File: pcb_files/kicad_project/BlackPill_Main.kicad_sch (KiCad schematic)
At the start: 2 parts

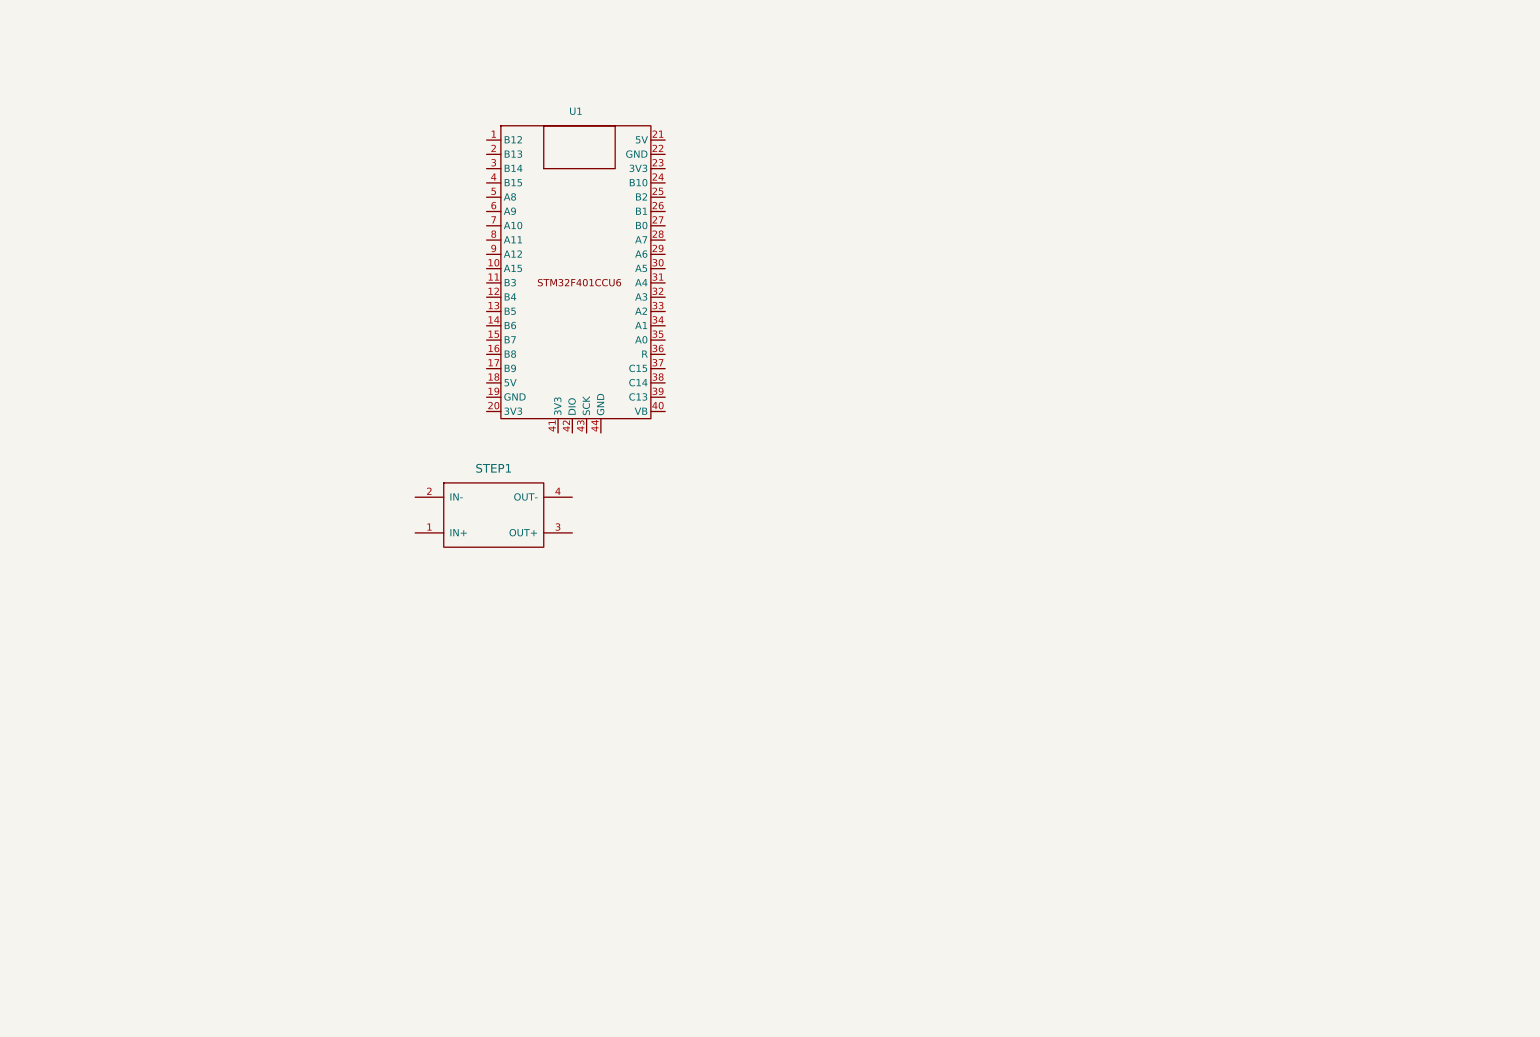
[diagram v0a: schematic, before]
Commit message: Añade pinout de BlackPill, completa esquemático y asocia footprints
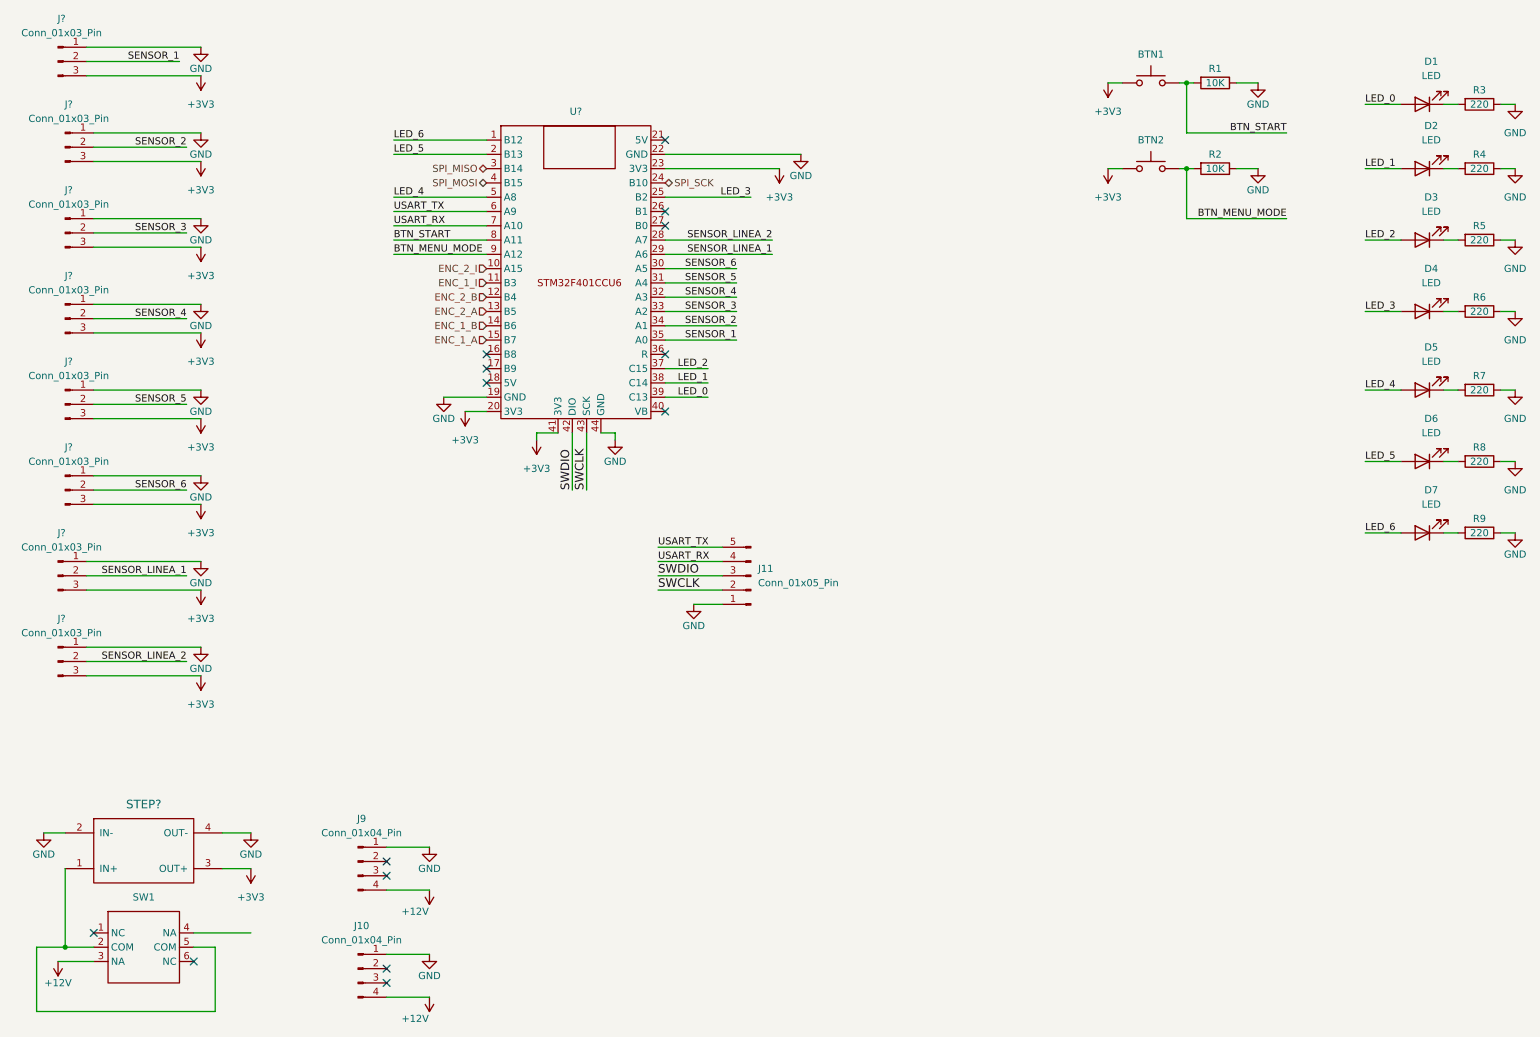
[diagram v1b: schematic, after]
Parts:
- added BTN1, BTN2: ~, Button_Switch_SMD:SW_SPST_EVQPE1, symbol custom_libraries:Button
- added D1, D2, D3, D4, D5, D6, D7: LED, LED_SMD:LED_0805_2012Metric, symbol Device:LED
- added J10, J9: Conn_01x04_Pin, Connector_PinHeader_2.54mm:PinHeader_1x04_P2.54mm_Vertical, symbol Connector:Conn_01x04_Pin
- added J11: Conn_01x05_Pin, Connector_PinHeader_2.54mm:PinHeader_1x05_P2.54mm_Vertical, symbol Connector:Conn_01x05_Pin
- added J? (x8): Conn_01x03_Pin, Connector_PinHeader_2.54mm:PinHeader_1x03_P2.54mm_Vertical, symbol Connector:Conn_01x03_Pin
- added R1, R2: 10K, Resistor_SMD:R_0805_2012Metric_Pad1.20x1.40mm_HandSolder, symbol Device:R
- added R3, R4, R5, R6, R7, R8, R9: 220, Resistor_SMD:R_0805_2012Metric_Pad1.20x1.40mm_HandSolder, symbol Device:R
- added SW1: ~, custom_library:Switch6P, symbol custom_libraries:Switch
- STEP?: renamed from STEP1; footprint (none) -> custom_library:Mini360
- U?: renamed from U1; footprint (none) -> custom_library:BlackPill_STM32F401
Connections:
- net at STEP?.1 (IN+): now also SW1.2 (COM), SW1.5 (COM)
- net GND: now reaches STEP?.2 (IN-)
- net GND: now also STEP?.4 (OUT-), U?.19 (GND), U?.22 (GND), U?.44 (GND), J10.1 (Pin_1), J11.1 (Pin_1), J9.1 (Pin_1), J?.1 (Pin_1), J?.1 (Pin_1), J?.1 (Pin_1), J?.1 (Pin_1), J?.1 (Pin_1), J?.1 (Pin_1), J?.1 (Pin_1), J?.1 (Pin_1), R1.1, R2.1, R3.1, R4.1, R5.1, R6.1, R7.1, R8.1, R9.1
- net +3V3: now reaches STEP?.3 (OUT+)
- net +3V3: now also U?.20 (3V3), U?.23 (3V3), U?.41 (3V3), BTN1.1, BTN2.1, J?.3 (Pin_3), J?.3 (Pin_3), J?.3 (Pin_3), J?.3 (Pin_3), J?.3 (Pin_3), J?.3 (Pin_3), J?.3 (Pin_3), J?.3 (Pin_3)
- net LED_6: now reaches U?.1 (B12)
- net LED_6: now also D7.2 (A)
- net ENC_2_I: now reaches U?.10 (A15)
- net ENC_1_I: now reaches U?.11 (B3)
- net ENC_2_B: now reaches U?.12 (B4)
- net ENC_2_A: now reaches U?.13 (B5)
- net ENC_1_B: now reaches U?.14 (B6)
- net ENC_1_A: now reaches U?.15 (B7)
- net LED_5: now reaches U?.2 (B13)
- net LED_5: now also D6.2 (A)
- net SPI_SCK: now reaches U?.24 (B10)
- net LED_3: now reaches U?.25 (B2)
- net LED_3: now also D4.2 (A)
- net SENSOR_LINEA_2: now reaches U?.28 (A7)
- net SENSOR_LINEA_2: now also J?.2 (Pin_2)
- net SENSOR_LINEA_1: now reaches U?.29 (A6)
- net SENSOR_LINEA_1: now also J?.2 (Pin_2)
- net SPI_MISO: now reaches U?.3 (B14)
- net SENSOR_6: now reaches U?.30 (A5)
- net SENSOR_6: now also J?.2 (Pin_2)
- net SENSOR_5: now reaches U?.31 (A4)
- net SENSOR_5: now also J?.2 (Pin_2)
- net SENSOR_4: now reaches U?.32 (A3)
- net SENSOR_4: now also J?.2 (Pin_2)
- net SENSOR_3: now reaches U?.33 (A2)
- net SENSOR_3: now also J?.2 (Pin_2)
- net SENSOR_2: now reaches U?.34 (A1)
- net SENSOR_2: now also J?.2 (Pin_2)
- net SENSOR_1: now reaches U?.35 (A0)
- net SENSOR_1: now also J?.2 (Pin_2)
- net LED_2: now reaches U?.37 (C15)
- net LED_2: now also D3.2 (A)
- net LED_1: now reaches U?.38 (C14)
- net LED_1: now also D2.2 (A)
- net LED_0: now reaches U?.39 (C13)
- net LED_0: now also D1.2 (A)
- net SPI_MOSI: now reaches U?.4 (B15)
- net SWDIO: now reaches U?.42 (DIO)
- net SWDIO: now also J11.3 (Pin_3)
- net SWCLK: now reaches U?.43 (SCK)
- net SWCLK: now also J11.2 (Pin_2)
- net LED_4: now reaches U?.5 (A8)
- net LED_4: now also D5.2 (A)
- net USART_TX: now reaches U?.6 (A9)
- net USART_TX: now also J11.5 (Pin_5)
- net USART_RX: now reaches U?.7 (A10)
- net USART_RX: now also J11.4 (Pin_4)
- net BTN_START: now reaches U?.8 (A11)
- net BTN_START: now also BTN1.2, R1.2
- net BTN_MENU_MODE: now reaches U?.9 (A12)
- net BTN_MENU_MODE: now also BTN2.2, R2.2
- new net: D2.1 (K), R4.2
- new net: D5.1 (K), R7.2
- new net: D4.1 (K), R6.2
- new net: D7.1 (K), R9.2
- new net: D3.1 (K), R5.2
- new net: D1.1 (K), R3.2
- new net: D6.1 (K), R8.2
- new net +12V: J10.4 (Pin_4), J9.4 (Pin_4), SW1.3 (NA)
- no-connect marks 0 -> 14
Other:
- moved on the sheet: STEP?

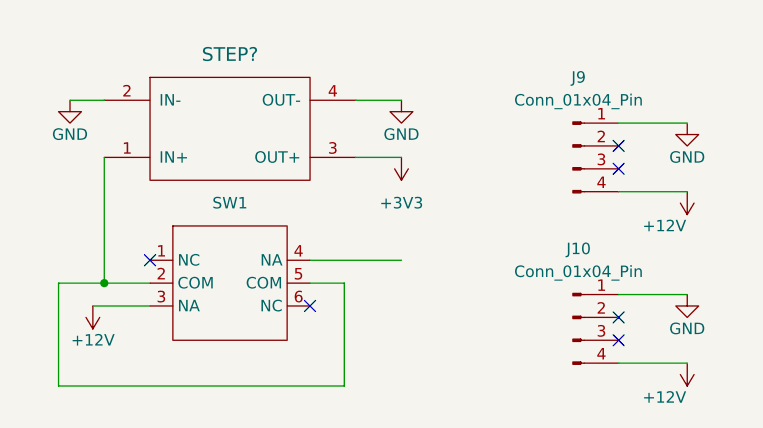
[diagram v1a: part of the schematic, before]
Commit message: Actualiza estructura del proyecto (symbols, footprints) y rutas relativas
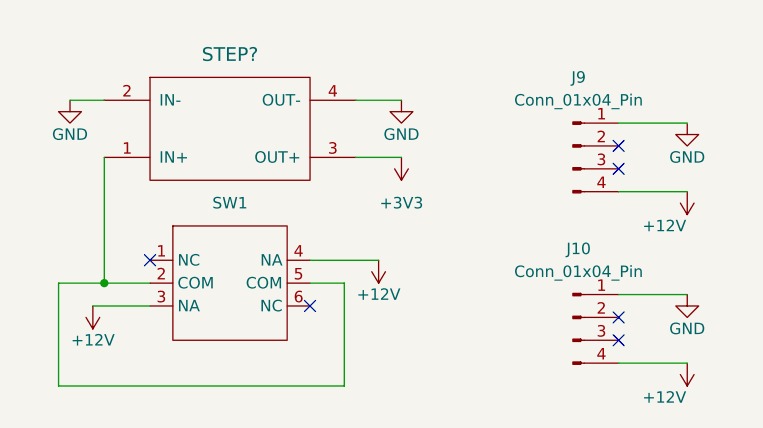
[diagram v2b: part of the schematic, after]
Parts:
- BTN1, BTN2: symbol custom_libraries:Button -> custom_symbols:Button
- STEP?: footprint custom_library:Mini360 -> custom_symbols:Mini360; symbol custom_libraries:Mini360 -> custom_symbols:Mini360
- SW1: footprint custom_library:Switch6P -> custom_symbols:Switch6P; symbol custom_libraries:Switch -> custom_symbols:Switch
- U?: footprint custom_library:BlackPill_STM32F401 -> custom_symbols:BlackPill_STM32F401; symbol custom_libraries:BlackPill -> custom_symbols:BlackPill
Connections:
- net +12V: now also SW1.4 (NA)
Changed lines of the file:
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@@
     (stroke (width 0) (type default))
   )
-  (wire (pts (xy 55.88 179.07) (xy 45.72 179.07))
+  (wire (pts (xy 53.34 179.07) (xy 45.72 179.07))
     (stroke (width 0) (type default))
   )
@@
     )
   )
-  (symbol (lib_id "custom_libraries:Mini360") (at 36.83 165.1 0) (unit 1)
+  (symbol (lib_id "custom_symbols:Mini360") (at 36.83 165.1 0) (unit 1)
     (in_bom yes) (on_board yes) (dnp no) (fields_autoplaced)
     (property "Reference" "STEP?" (at 36.83 156.21 0)
@@
       (effects (font (size 1.524 1.524)))
     )
-    (property "Footprint" "custom_library:Mini360" (at 36.83 163.83 0)
+    (property "Footprint" "custom_symbols:Mini360" (at 36.83 163.83 0)
       (effects (font (size 1.524 1.524)) hide)
     )
@@
     )
   )
-  (symbol (lib_id "custom_libraries:Button") (at 215.9 43.18 0) (unit 1)
+  (symbol (lib_id "custom_symbols:Button") (at 215.9 43.18 0) (unit 1)
     (in_bom yes) (on_board yes) (dnp no) (fields_autoplaced)
     (property "Reference" "BTN2" (at 215.9 38.1 0)
@@
     )
   )
-  (symbol (lib_id "custom_libraries:Switch") (at 36.83 181.61 0) (unit 1)
+  (symbol (lib_id "custom_symbols:Switch") (at 36.83 181.61 0) (unit 1)
     (in_bom yes) (on_board yes) (dnp no) (fields_autoplaced)
     (property "Reference" "SW1" (at 36.83 172.72 0)
@@
       (effects (font (size 1.27 1.27)))
     )
-    (property "Footprint" "custom_library:Switch6P" (at 36.83 181.61 0)
+    (property "Footprint" "custom_symbols:Switch6P" (at 36.83 181.61 0)
       (effects (font (size 1.27 1.27)) hide)
     )
@@
     )
   )
+  (symbol (lib_id "power:+12V") (at 53.34 179.07 180) (unit 1)
+    (in_bom yes) (on_board yes) (dnp no)
+    (property "Reference" "#PWR?" (at 53.34 175.26 0)
+      (effects (font (size 1.27 1.27)) hide)
+    )
+    (property "Value" "+12V" (at 53.34 182.88 0)
+      (effects (font (size 1.27 1.27)))
+    )
+    (property "Footprint" "" (at 53.34 179.07 0)
+      (effects (font (size 1.27 1.27)) hide)
+    )
+    (property "Datasheet" "" (at 53.34 179.07 0)
+      (effects (font (size 1.27 1.27)) hide)
+    )
+    (pin "1")
+    (instances
+      (project "UltiBot"
+        (path "/24197ddb-6745-4cc2-89a2-3cda2c96a453/801aac4b-54d6-4691-9ae2-22a76f924486"
+          (reference "#PWR?") (unit 1)
+        )
+        (path "/24197ddb-6745-4cc2-89a2-3cda2c96a453/922bab18-0964-4bd0-af02-17c76d29e803"
+          (reference "#PWR071") (unit 1)
+        )
+      )
+    )
+  )
   (symbol (lib_id "Device:R") (at 274.32 31.75 270) (unit 1)
     (in_bom yes) (on_board yes) (dnp no)
@@
     )
   )
-  (symbol (lib_id "custom_libraries:Button") (at 215.9 27.94 0) (unit 1)
+  (symbol (lib_id "custom_symbols:Button") (at 215.9 27.94 0) (unit 1)
     (in_bom yes) (on_board yes) (dnp no) (fields_autoplaced)
     (property "Reference" "BTN1" (at 215.9 22.86 0)
@@
     )
   )
-  (symbol (lib_id "custom_libraries:BlackPill") (at 114.3 63.5 0) (unit 1)
+  (symbol (lib_id "custom_symbols:BlackPill") (at 114.3 63.5 0) (unit 1)
     (in_bom yes) (on_board yes) (dnp no) (fields_autoplaced)
     (property "Reference" "U?" (at 113.665 33.02 0)
@@
       (effects (font (size 1.27 1.27)))
     )
-    (property "Footprint" "custom_library:BlackPill_STM32F401" (at 114.3 63.5 0)
-      (effects (font (size 1.27 1.27)) hide)
-    )
+    (property "Footprint" "custom_symbols:BlackPill_STM32F401" (at 114.3 63.5 0)
+      (effects (font (size 1.27 1.27)) hide)
+    )
